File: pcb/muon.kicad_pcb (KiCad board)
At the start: 2 copper layers, 72 x 55 mm, 61 parts, among them J1 Debug Pins, J2 USB_C_Receptacle_USB2.0, SW1 Kailh Hotswap, SW2 Kailh Hotswap, SW3 Reset, SW4 DTSM-66R-V-T/R, SW5 DTSM-66R-V-T/R, SW6 DTSM-66R-V-T/R, SW7 Kailh Hotswap, U1 SRV05-4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

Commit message: Move USB closer to the edge of the case Add gitignore
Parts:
- moved J2 3.90 mm to (153.5, 53.4)
- moved R3 2.37 mm to (149.7, 62.3)
- moved U1 2.15 mm to (152.8, 63.0)
- moved R4 1.99 mm to (156.0, 62.3)
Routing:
- net /D-: track 28.0 -> 30.1 mm
- net /VBUS_: track 19.6 -> 21.6 mm
- net Net-(J2-PadB5): track 2.95 -> 4.62 mm
- net /D+: track 26.3 -> 25.3 mm
- net GND: track 17.7 -> 18.5 mm, vias 21 -> 28
- net Net-(J2-PadA5): track 5.12 -> 5.80 mm
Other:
- board size 72 x 55 mm -> 72 x 59 mm

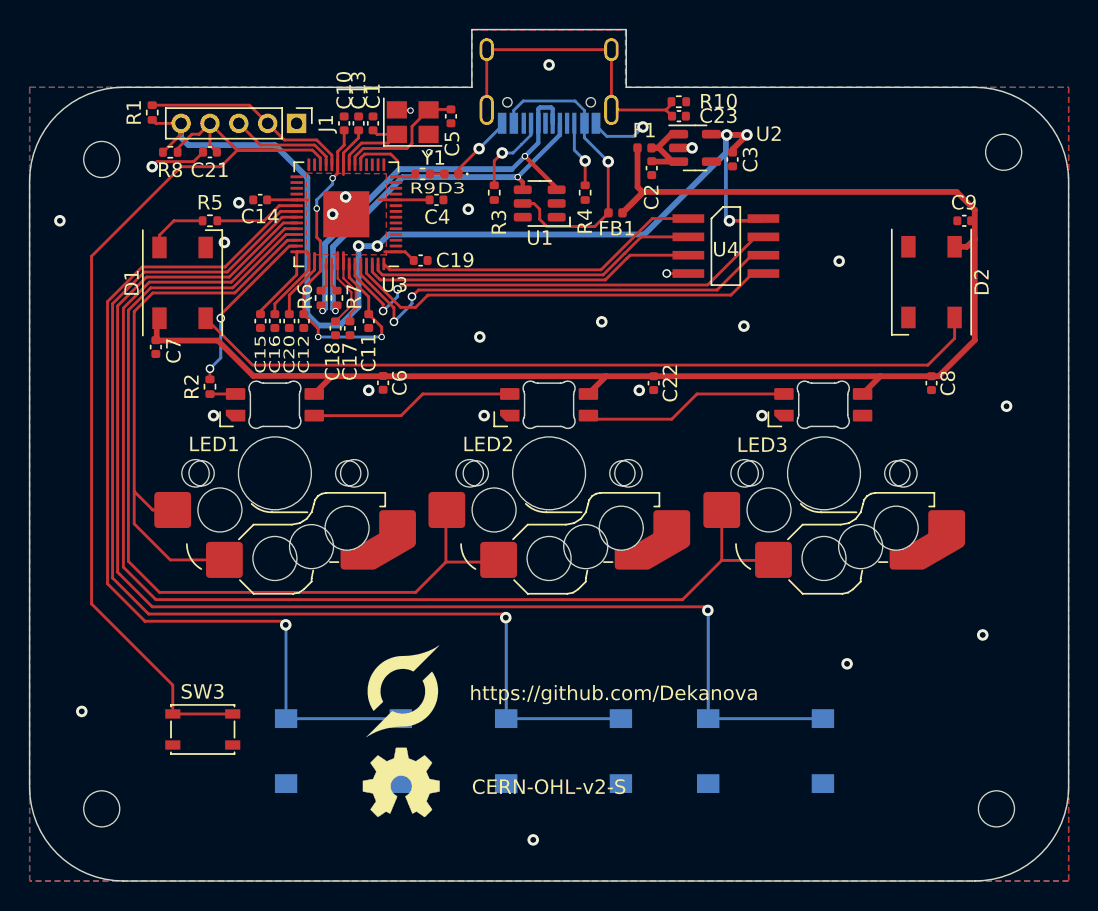
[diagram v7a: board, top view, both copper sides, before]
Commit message: Change buttons and move them into place Update 3D models
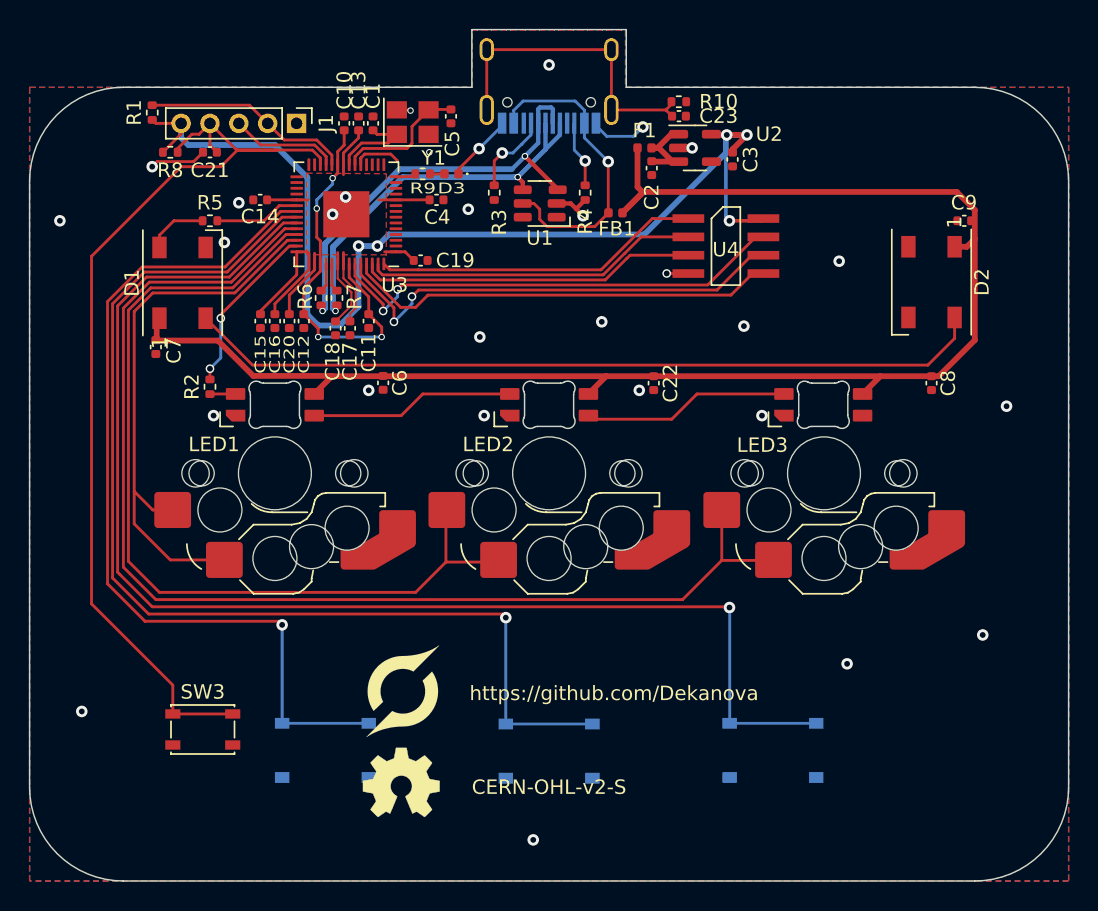
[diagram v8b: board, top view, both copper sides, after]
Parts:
- removed REF** (x4): MountingHole_2.5mm, MountingHole:MountingHole_2.5mm
- removed SW4, SW5, SW6: DTSM-66R-V-T/R, Button_Switch_SMD:SW_Push_1P1T_NO_6x6mm_H9.5mm
- added S1: TS-1187A-B-A-B, button:SW_TS-1187A-B-A-B, B.Cu at (138.0, 101.0)
- added S2: TS-1187A-B-A-B, button:SW_TS-1187A-B-A-B, B.Cu at (153.5, 101.0)
- added S3: TS-1187A-B-A-B, button:SW_TS-1187A-B-A-B, B.Cu at (169.0, 101.0)
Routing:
- net /D+: track 25.3 -> 29.8 mm
- net GND: track 18.5 -> 21.6 mm, vias 28 -> 29
- net /FN1: track 63.2 -> 61.4 mm
- net /FN2: track 77.6 -> 76.0 mm
